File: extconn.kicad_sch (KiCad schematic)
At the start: 23 parts, among them J1401 Conn_02x10_Odd_Even, U1401 74AVC4T245PW, U1402 74AVC4T245PW

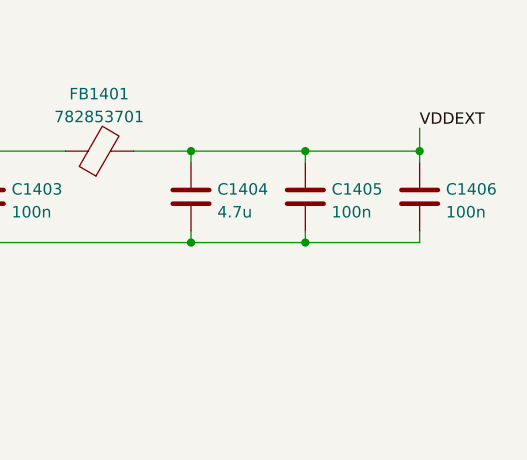
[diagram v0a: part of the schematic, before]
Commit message: Extconn: remove redundant 100n cap
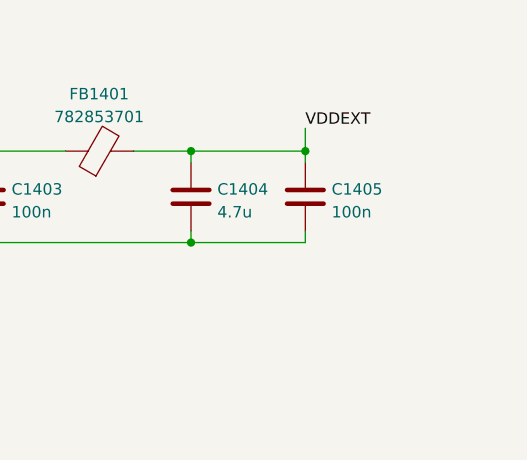
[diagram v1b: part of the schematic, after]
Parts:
- removed C1406: 100n, Capacitor_SMD:C_0805_2012Metric, symbol Device:C
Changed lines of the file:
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@@
   (junction (at 238.76 48.26) (diameter 0) (color 0 0 0 0)
   )
-  (junction (at 264.16 38.1) (diameter 0) (color 0 0 0 0)
-  )
   (junction (at 215.9 38.1) (diameter 0) (color 0 0 0 0)
   )
-  (junction (at 251.46 48.26) (diameter 0) (color 0 0 0 0)
-  )
   (junction (at 186.69 125.73) (diameter 0) (color 0 0 0 0)
   )
   (junction (at 186.69 128.27) (diameter 0) (color 0 0 0 0)
   )
+  (junction (at 251.46 38.1) (diameter 0) (color 0 0 0 0)
+  )
   (junction (at 186.69 135.89) (diameter 0) (color 0 0 0 0)
   )
@@
   (junction (at 186.69 133.35) (diameter 0) (color 0 0 0 0)
   )
-  (junction (at 251.46 38.1) (diameter 0) (color 0 0 0 0)
-  )
   (junction (at 83.82 88.9) (diameter 0) (color 0 0 0 0)
   )
@@
     (stroke (width 0) (type default) (color 0 0 0 0))
   )
-  (wire (pts (xy 264.16 46.99) (xy 264.16 48.26))
-    (stroke (width 0) (type default) (color 0 0 0 0))
-  )
   (wire (pts (xy 99.06 160.02) (xy 99.06 161.29))
     (stroke (width 0) (type default) (color 0 0 0 0))
@@
     (stroke (width 0) (type default) (color 0 0 0 0))
   )
-  (wire (pts (xy 264.16 39.37) (xy 264.16 38.1))
-    (stroke (width 0) (type default) (color 0 0 0 0))
-  )
   (wire (pts (xy 171.45 118.11) (xy 167.64 118.11))
     (stroke (width 0) (type default) (color 0 0 0 0))
@@
     (stroke (width 0) (type default) (color 0 0 0 0))
   )
-  (wire (pts (xy 264.16 35.56) (xy 264.16 38.1))
+  (wire (pts (xy 251.46 35.56) (xy 251.46 38.1))
     (stroke (width 0) (type default) (color 0 0 0 0))
   )
@@
     (stroke (width 0) (type default) (color 0 0 0 0))
   )
-  (wire (pts (xy 251.46 48.26) (xy 264.16 48.26))
-    (stroke (width 0) (type default) (color 0 0 0 0))
-  )
   (wire (pts (xy 88.9 40.64) (xy 88.9 41.91))
     (stroke (width 0) (type default) (color 0 0 0 0))
@@
   )
   (wire (pts (xy 168.91 115.57) (xy 168.91 110.49))
-    (stroke (width 0) (type default) (color 0 0 0 0))
-  )
-  (wire (pts (xy 264.16 38.1) (xy 251.46 38.1))
     (stroke (width 0) (type default) (color 0 0 0 0))
   )
@@
     (effects (font (size 1.27 1.27)) (justify left bottom))
   )
-  (label "VDDEXT" (at 264.16 35.56 0)
+  (label "VDDEXT" (at 251.46 35.56 0)
     (effects (font (size 1.27 1.27)) (justify left bottom))
   )
@@
       (effects (font (size 1.27 1.27)) hide)
     )
-    (pin "1")
-    (pin "2")
-  )
-  (symbol (lib_id "Device:C") (at 264.16 43.18 0) (unit 1)
-    (in_bom yes) (on_board yes) (fields_autoplaced)
-    (property "Reference" "C1406" (id 0) (at 267.081 42.3453 0)
-      (effects (font (size 1.27 1.27)) (justify left))
-    )
-    (property "Value" "100n" (id 1) (at 267.081 44.8822 0)
-      (effects (font (size 1.27 1.27)) (justify left))
-    )
-    (property "Footprint" "Capacitor_SMD:C_0805_2012Metric" (id 2) (at 265.1252 46.99 0)
-      (effects (font (size 1.27 1.27)) hide)
-    )
-    (property "Datasheet" "~" (id 3) (at 264.16 43.18 0)
-      (effects (font (size 1.27 1.27)) hide)
-    )
-    (property "Spec1" "" (id 4) (at 264.16 43.18 0)
-      (effects (font (size 1.27 1.27)) hide)
-    )
-    (property "Spec2" "" (id 5) (at 264.16 43.18 0)
-      (effects (font (size 1.27 1.27)) hide)
-    )
-    (property "Tolerance" "" (id 6) (at 264.16 43.18 0)
-      (effects (font (size 1.27 1.27)) hide)
-    )
-    (property "Mfr" "Samsung" (id 7) (at 264.16 43.18 0)
-      (effects (font (size 1.27 1.27)) hide)
-    )
-    (property "Mfr PN" "CL21B104KBFNNNE" (id 8) (at 264.16 43.18 0)
-      (effects (font (size 1.27 1.27)) hide)
-    )

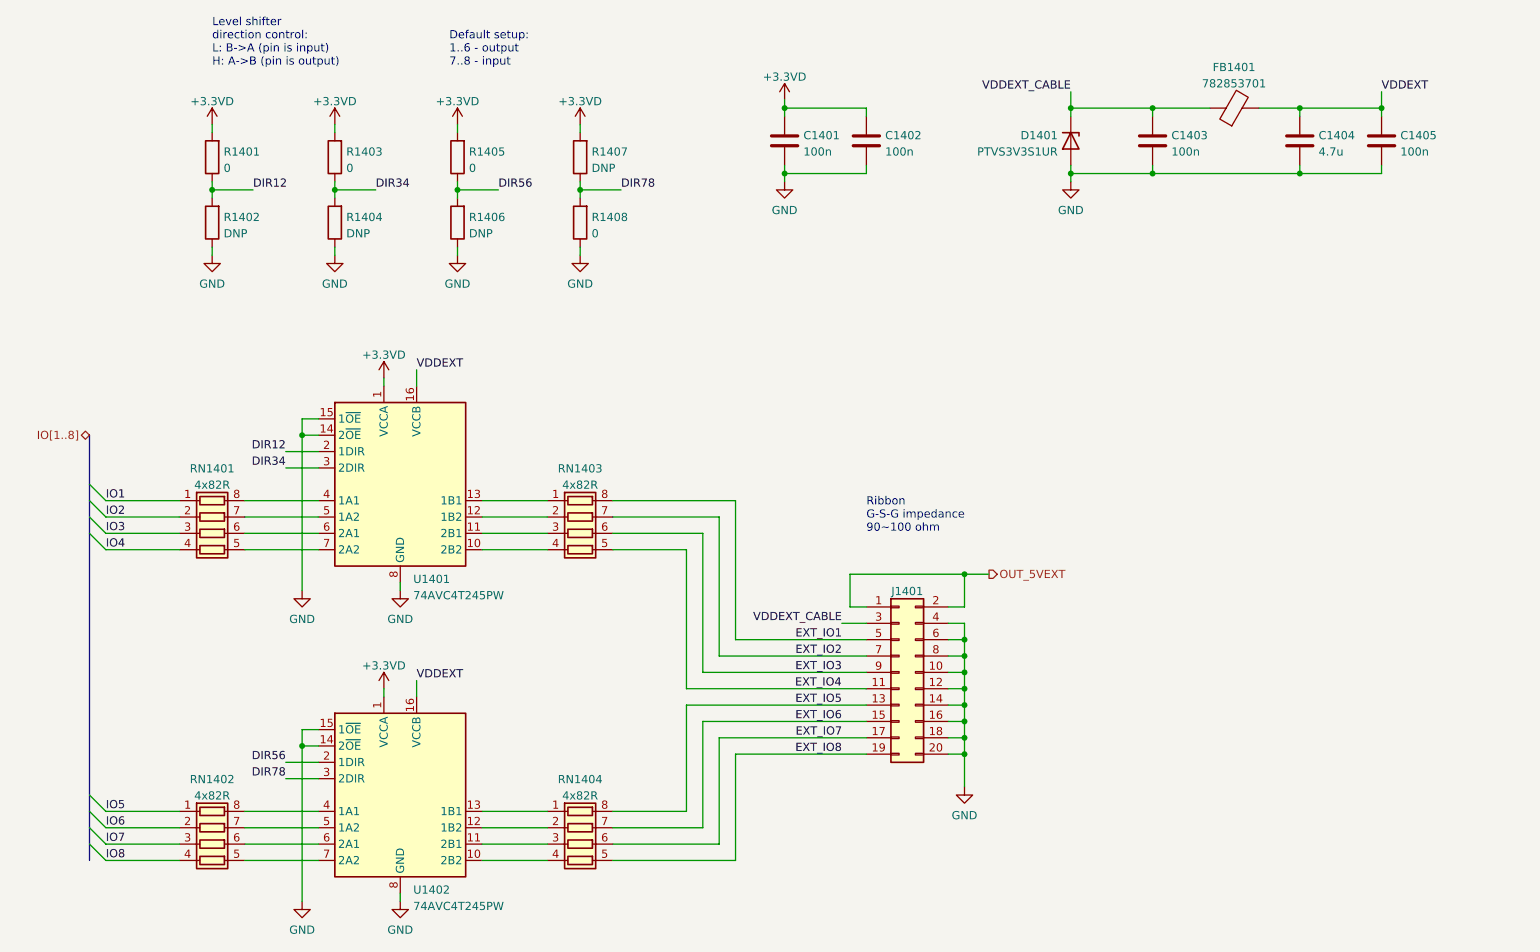
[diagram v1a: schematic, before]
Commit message: extconn: add 3v3d output
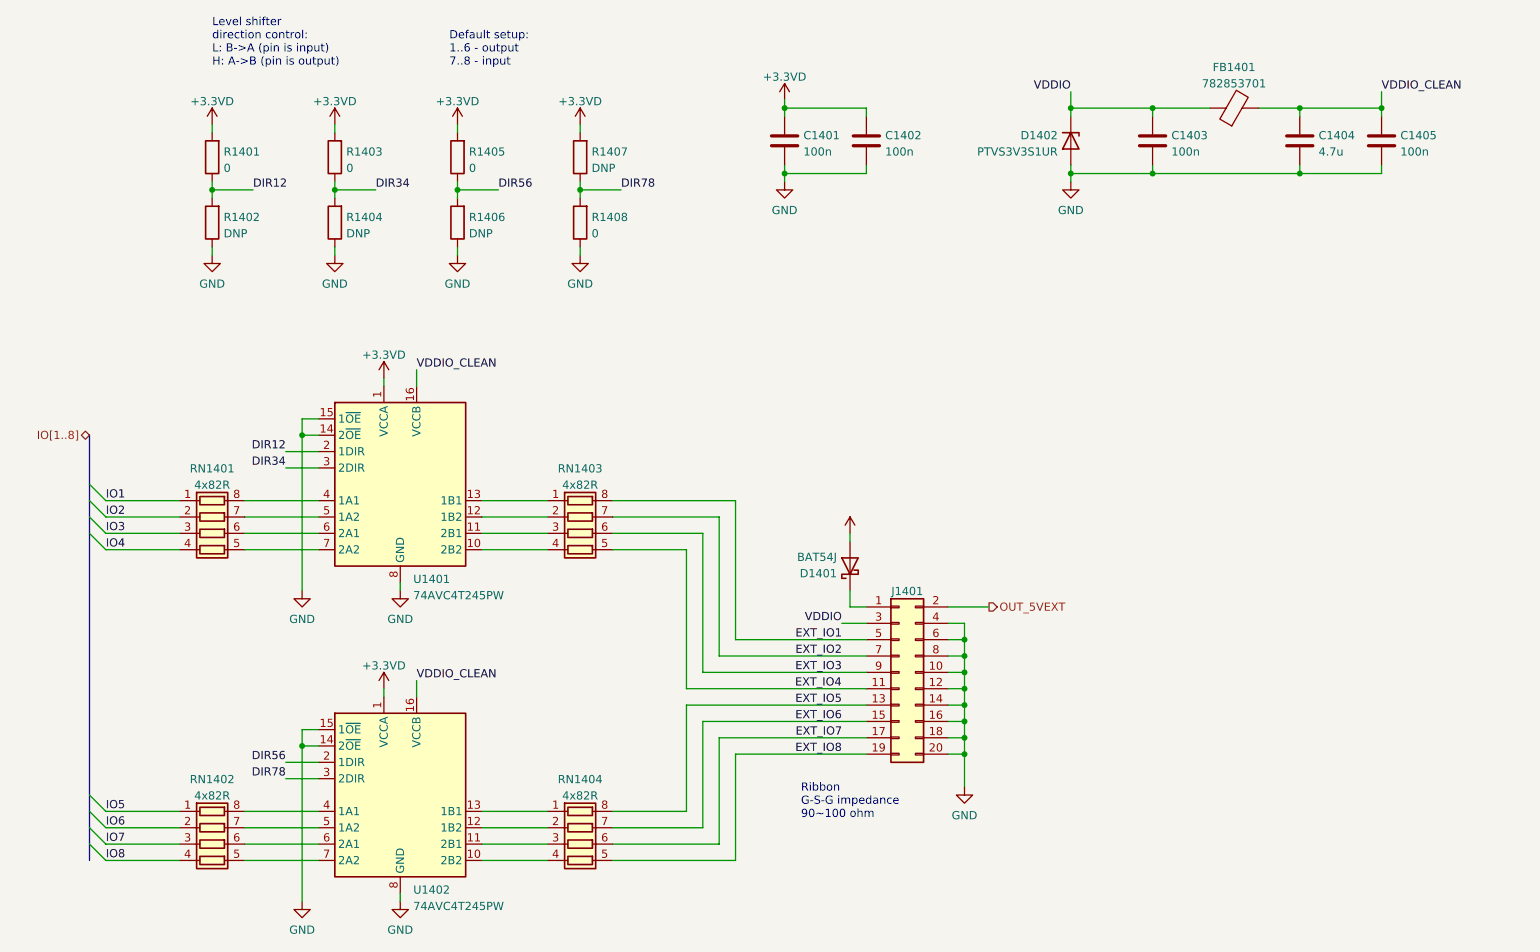
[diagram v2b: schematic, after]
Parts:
- added D1401: BAT54J, Diode_SMD:D_SOD-323F, symbol Diode:BAT54J
- renumbered D1401 to D1402
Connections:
- net +3.3VD: now also D1401.2 (A)
- net OUT_5VEXT: no longer J1401.1 (Pin_1)
- net VDDEXT renamed VDDIO_CLEAN
- net VDDEXT_CABLE renamed VDDIO
- new net: D1401.1 (K), J1401.1 (Pin_1)
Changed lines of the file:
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@@
   (junction (at 83.82 137.16) (diameter 0) (color 0 0 0 0)
   )
-  (junction (at 186.69 110.49) (diameter 0) (color 0 0 0 0)
-  )
   (junction (at 127 50.8) (diameter 0) (color 0 0 0 0)
   )
@@
     (stroke (width 0) (type default) (color 0 0 0 0))
   )
-  (wire (pts (xy 168.91 110.49) (xy 186.69 110.49))
-    (stroke (width 0) (type default) (color 0 0 0 0))
-  )
   (wire (pts (xy 203.2 48.26) (xy 203.2 49.53))
     (stroke (width 0) (type default) (color 0 0 0 0))
@@
     (stroke (width 0) (type default) (color 0 0 0 0))
   )
-  (wire (pts (xy 186.69 110.49) (xy 190.5 110.49))
-    (stroke (width 0) (type default) (color 0 0 0 0))
-  )
   (wire (pts (xy 74.93 152.4) (xy 86.36 152.4))
     (stroke (width 0) (type default) (color 0 0 0 0))
@@
     (stroke (width 0) (type default) (color 0 0 0 0))
   )
+  (wire (pts (xy 168.91 115.57) (xy 171.45 115.57))
+    (stroke (width 0) (type default) (color 0 0 0 0))
+  )
   (wire (pts (xy 53.34 106.68) (xy 64.77 106.68))
     (stroke (width 0) (type default) (color 0 0 0 0))
@@
     (stroke (width 0) (type default) (color 0 0 0 0))
   )
+  (wire (pts (xy 168.91 113.03) (xy 168.91 115.57))
+    (stroke (width 0) (type default) (color 0 0 0 0))
+  )
   (wire (pts (xy 53.34 104.14) (xy 64.77 104.14))
     (stroke (width 0) (type default) (color 0 0 0 0))
@@
     (stroke (width 0) (type default) (color 0 0 0 0))
   )
-  (wire (pts (xy 186.69 115.57) (xy 184.15 115.57))
+  (wire (pts (xy 184.15 115.57) (xy 190.5 115.57))
     (stroke (width 0) (type default) (color 0 0 0 0))
   )
@@
     (stroke (width 0) (type default) (color 0 0 0 0))
   )
-  (wire (pts (xy 186.69 110.49) (xy 186.69 115.57))
-    (stroke (width 0) (type default) (color 0 0 0 0))
-  )
   (wire (pts (xy 203.2 38.1) (xy 203.2 39.37))
     (stroke (width 0) (type default) (color 0 0 0 0))
@@
     (stroke (width 0) (type default) (color 0 0 0 0))
   )
-  (wire (pts (xy 171.45 115.57) (xy 168.91 115.57))
-    (stroke (width 0) (type default) (color 0 0 0 0))
-  )
   (wire (pts (xy 184.15 133.35) (xy 186.69 133.35))
     (stroke (width 0) (type default) (color 0 0 0 0))
@@
     (stroke (width 0) (type default) (color 0 0 0 0))
   )
+  (wire (pts (xy 168.91 104.14) (xy 168.91 105.41))
+    (stroke (width 0) (type default) (color 0 0 0 0))
+  )
   (wire (pts (xy 132.08 152.4) (xy 148.59 152.4))
     (stroke (width 0) (type default) (color 0 0 0 0))
@@
     (stroke (width 0) (type default) (color 0 0 0 0))
   )
-  (wire (pts (xy 168.91 115.57) (xy 168.91 110.49))
-    (stroke (width 0) (type default) (color 0 0 0 0))
-  )
   (wire (pts (xy 69.85 49.53) (xy 69.85 50.8))
     (stroke (width 0) (type default) (color 0 0 0 0))
@@
     (stroke (width 0) (type default) (color 0 0 0 0))
   )
-  (text "Ribbon\nG-S-G impedance\n90~100 ohm" (at 171.45 104.14 0)
+  (text "Ribbon\nG-S-G impedance\n90~100 ohm" (at 161.29 148.59 0)
     (effects (font (size 1.27 1.27)) (justify left bottom))
   )
@@
     (effects (font (size 1.27 1.27)) (justify right bottom))
   )
-  (label "VDDEXT_CABLE" (at 167.64 118.11 180)
+  (label "VDDIO" (at 167.64 118.11 180)
     (effects (font (size 1.27 1.27)) (justify right bottom))
   )
@@
     (effects (font (size 1.27 1.27)) (justify left bottom))
   )
-  (label "VDDEXT" (at 251.46 35.56 0)
+  (label "VDDIO_CLEAN" (at 251.46 35.56 0)
     (effects (font (size 1.27 1.27)) (justify left bottom))
   )
@@
     (effects (font (size 1.27 1.27)) (justify right bottom))
   )
-  (label "VDDEXT_CABLE" (at 203.2 35.56 180)
+  (label "VDDIO" (at 203.2 35.56 180)
     (effects (font (size 1.27 1.27)) (justify right bottom))
   )
@@
     (effects (font (size 1.27 1.27)) (justify left bottom))
   )
-  (label "VDDEXT" (at 101.6 78.74 0)
+  (label "VDDIO_CLEAN" (at 101.6 78.74 0)
     (effects (font (size 1.27 1.27)) (justify left bottom))
   )
@@
     (effects (font (size 1.27 1.27)) (justify left bottom))
   )
-  (label "VDDEXT" (at 101.6 127 0)
+  (label "VDDIO_CLEAN" (at 101.6 127 0)
     (effects (font (size 1.27 1.27)) (justify left bottom))
   )
@@
     (effects (font (size 1.27 1.27)) (justify right))
   )
-  (hierarchical_label "OUT_5VEXT" (shape output) (at 190.5 110.49 0)
+  (hierarchical_label "OUT_5VEXT" (shape output) (at 190.5 115.57 0)
     (effects (font (size 1.27 1.27)) (justify left))
   )
@@
   (symbol (lib_id "power:GND") (at 186.69 143.51 0) (unit 1)
     (in_bom yes) (on_board yes) (fields_autoplaced)
-    (property "Reference" "#PWR01417" (id 0) (at 186.69 149.86 0)
+    (property "Reference" "#PWR01418" (id 0) (at 186.69 149.86 0)
       (effects (font (size 1.27 1.27)) hide)
     )
@@
   (symbol (lib_id "Device:D_Zener") (at 203.2 43.18 270) (unit 1)
     (in_bom yes) (on_board yes) (fields_autoplaced)
-    (property "Reference" "D1401" (id 0) (at 201.1681 42.3453 90)
+    (property "Reference" "D1402" (id 0) (at 201.1681 42.3453 90)
       (effects (font (size 1.27 1.27)) (justify right))
     )
@@
   (symbol (lib_id "power:GND") (at 203.2 49.53 0) (unit 1)
     (in_bom yes) (on_board yes) (fields_autoplaced)
-    (property "Reference" "#PWR01418" (id 0) (at 203.2 55.88 0)
+    (property "Reference" "#PWR01419" (id 0) (at 203.2 55.88 0)
       (effects (font (size 1.27 1.27)) hide)
     )
@@
     (pin "8")
   )
+  (symbol (lib_id "symbols:+3.3VD") (at 168.91 104.14 0) (unit 1)
+    (in_bom yes) (on_board yes)
+    (property "Reference" "#PWR01417" (id 0) (at 168.91 107.95 0)
+      (effects (font (size 1.27 1.27)) hide)
+    )
+    (property "Value" "" (id 1) (at 168.91 100.584 0))
+    (property "Footprint" "" (id 2) (at 168.91 104.14 0)
+      (effects (font (size 1.27 1.27)) hide)
+    )
+    (property "Datasheet" "" (id 3) (at 168.91 104.14 0)
+      (effects (font (size 1.27 1.27)) hide)
+    )
+    (pin "1")
+  )
   (symbol (lib_id "Device:R") (at 88.9 45.72 180) (unit 1)
     (in_bom yes) (on_board yes) (fields_autoplaced)
@@
       (effects (font (size 1.27 1.27)) hide)
     )
+    (pin "1")
+    (pin "2")
+  )
+  (symbol (lib_id "Diode:BAT54J") (at 168.91 109.22 90) (unit 1)
+    (in_bom yes) (on_board yes) (fields_autoplaced)
+    (property "Reference" "D1401" (id 0) (at 166.878 110.3722 90)
+      (effects (font (size 1.27 1.27)) (justify left))
+    )
+    (property "Value" "BAT54J" (id 1) (at 166.878 107.8353 90)
+      (effects (font (size 1.27 1.27)) (justify left))
+    )
+    (property "Footprint" "Diode_SMD:D_SOD-323F" (id 2) (at 173.355 109.22 0)
+      (effects (font (size 1.27 1.27)) hide)
+    )
+    (property "Datasheet" "https://assets.nexperia.com/documents/data-sheet/BAT54J.pdf" (id 3) (at 168.91 109.22 0)
+      (effects (font (size 1.27 1.27)) hide)
+    )
+    (property "Mfr" "Nexperia" (id 4) (at 168.91 109.22 0)
+      (effects (font (size 1.27 1.27)) hide)
+    )
+    (property "Mfr PN" "BAT54HGWX" (id 5) (at 168.91 109.22 0)
+      (effects (font (size 1.27 1.27)) hide)
+    )

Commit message: Update schematic: - Redesign of decoupling based on swcad modelling (predominantly use 1uf, no paralleled caps) - Reroute REF_CLK_IN, CLK_SEL net to different FPGA pins - Some net renaming - Ext conn: add decoupling to 3v3 output - Reassign references to all components PCB: routing almost finished
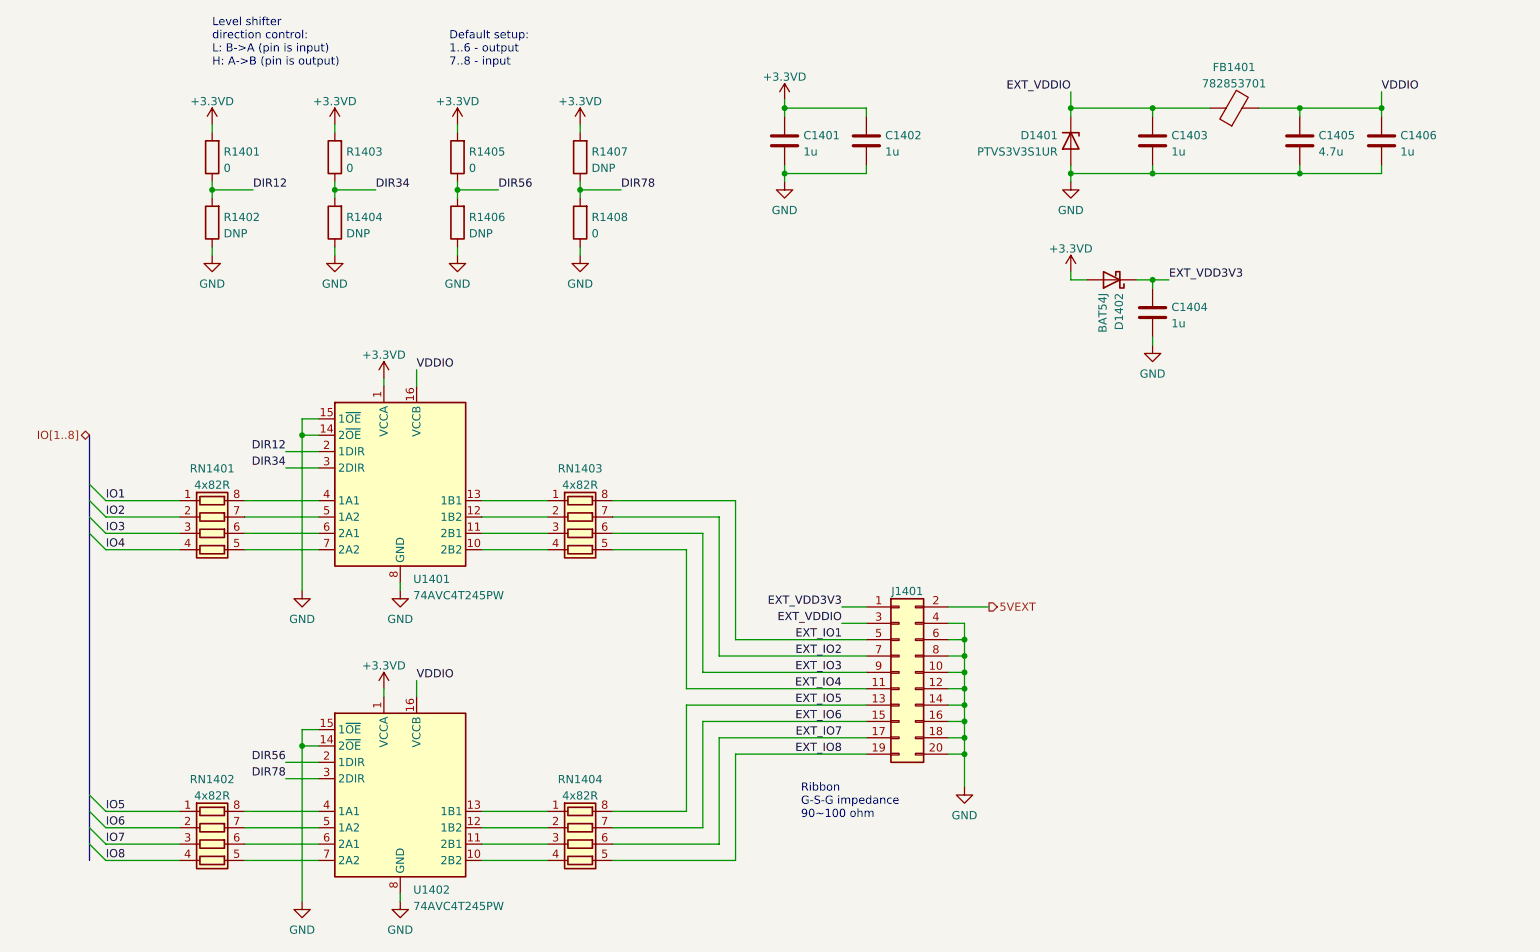
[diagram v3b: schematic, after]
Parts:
- removed C1405: 100n, Capacitor_SMD:C_0805_2012Metric, symbol Device:C
- added C1404, C1406: 1u, Capacitor_SMD:C_0805_2012Metric, symbol Device:C
- C1401, C1402, C1403: value 100n -> 1u; Mfr PN CL21B104KBFNNNE -> CL21B105KOFNNNG
- renumbered C1404 to C1405, D1402 to D1401, D1401 to D1402
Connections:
- net VDDIO_CLEAN is gone; now on net VDDIO: C1405.1, FB1401.2, U1401.16 (VCCB), U1402.16 (VCCB)
- net GND: now also C1404.2, C1406.2
- net VDDIO: now also C1406.1; no longer C1403.1, D1401.1 (K), FB1401.1, J1401.3 (Pin_3)
- net EXT_VDD3V3: now reaches D1402.1 (K), J1401.1 (Pin_1)
- net EXT_VDD3V3: now also C1404.1
- net OUT_5VEXT renamed 5VEXT
- new net EXT_VDDIO: C1403.1, D1401.1 (K), FB1401.1, J1401.3 (Pin_3)
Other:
- moved on the sheet: D1402
